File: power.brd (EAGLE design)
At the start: 37.8 x 80 mm, 56 parts, among them CON1 PINHEAD_2X02-0877590414, CON2 PINHEAD_2X02-0877590414, CON3 PINHEAD_2X02-0877590414, CON5 PINHEAD_2X02-0877590414, CON6 PINHEAD_2X04-SMD-2-MALE, IC1 UCC272-VDFN-HEAVY_PCB, IC2 UCC272-VDFN-HEAVY_PCB, IC3 UCC272-VDFN-HEAVY_PCB, Q101 BSC077N12NS3GATMA1, Q102 BSC077N12NS3GATMA1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

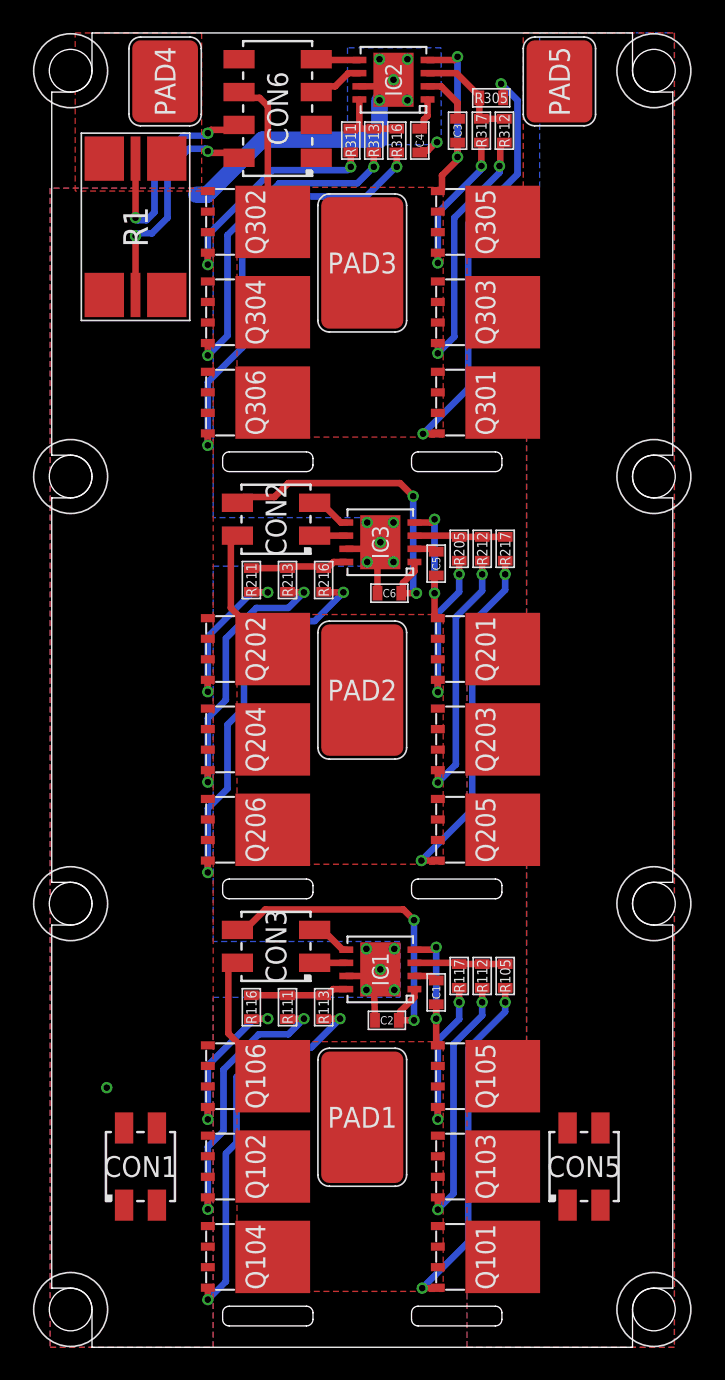
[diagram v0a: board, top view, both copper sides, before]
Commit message: pwr pcb routing completed
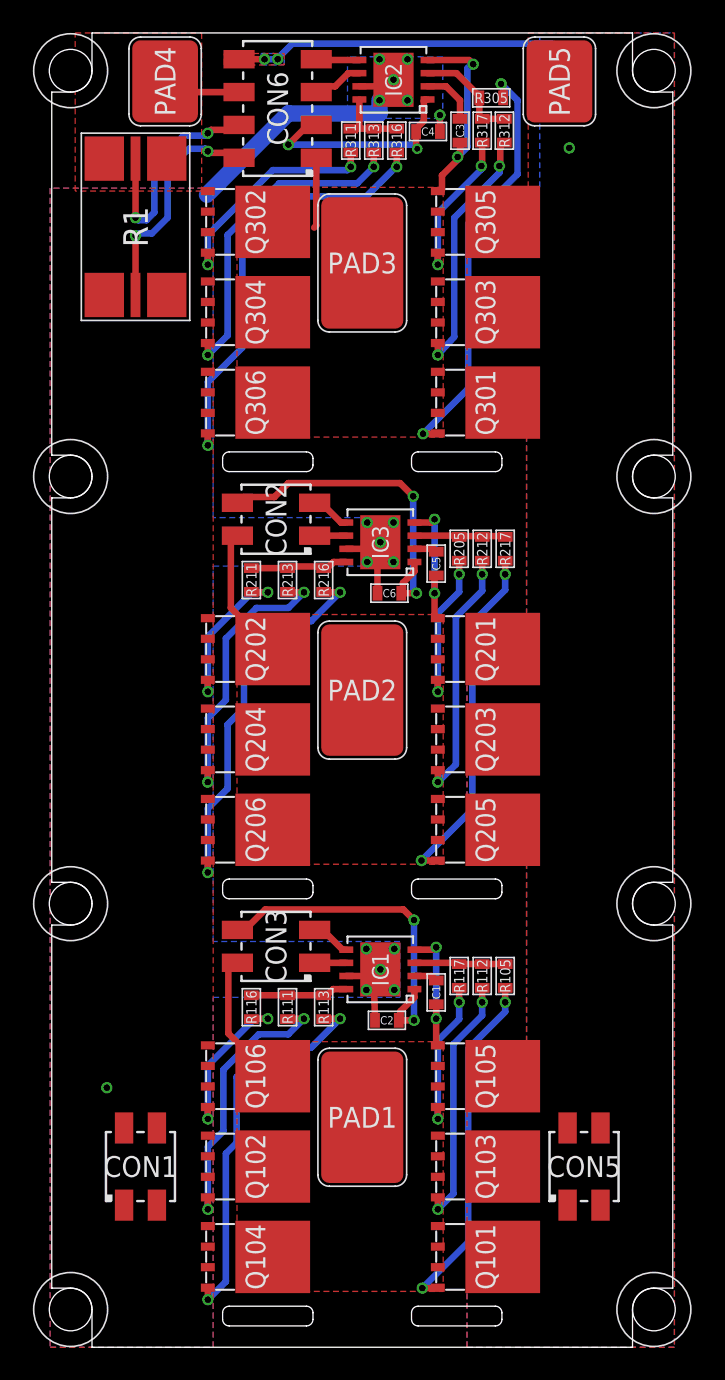
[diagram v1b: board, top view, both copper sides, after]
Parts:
- moved C4 0.74 mm to (4.00, 74.0), turned to 0 degrees
- moved C3 0.15 mm to (5.95, 74.0)
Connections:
- removed net N$7: PAD4.P$1, R1.1, R1.11
- new net VBAT-: CON6.6, PAD4.P$1, R1.1, R1.11
- net C_PH: now also CON6.1; no longer CON6.6
- net VDC: now also CON6.8
- net VDD_15V: now also CON6.3
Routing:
- net VDC: track 0.00 -> 19.5 mm, vias 0 -> 3
- net VDD_15V: track 43.8 -> 55.2 mm, vias 4 -> 6
- net VBAT-: track 0.00 -> 5.15 mm
- net C_PH: track 20.8 -> 17.0 mm
- net PGND: track 30.6 -> 28.0 mm
- added copper zone on layer 1, net VBAT-
- removed copper zone on layer 1, net N$7
